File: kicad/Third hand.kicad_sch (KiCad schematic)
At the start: 66 parts, among them U001 74HC595, U002 74HC595

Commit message: First completely routed version
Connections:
- net Px0 renamed Tx0
- net Px1 renamed Tx1
- net Px2 renamed Tx2
- net Px3 renamed Tx3
- net Px4 renamed Tx4
- net Px5 renamed Tx5
- net Px6 renamed Tx6
- net Px7 renamed Tx7
- net Px8 renamed Tx8
- net Px9 renamed Tx9
- net Q0x renamed T0x
- net Q1x renamed T1x
- net Q2x renamed T2x
- net Q3x renamed T3x
- net Q4x renamed T4x
- net Q5x renamed T5x

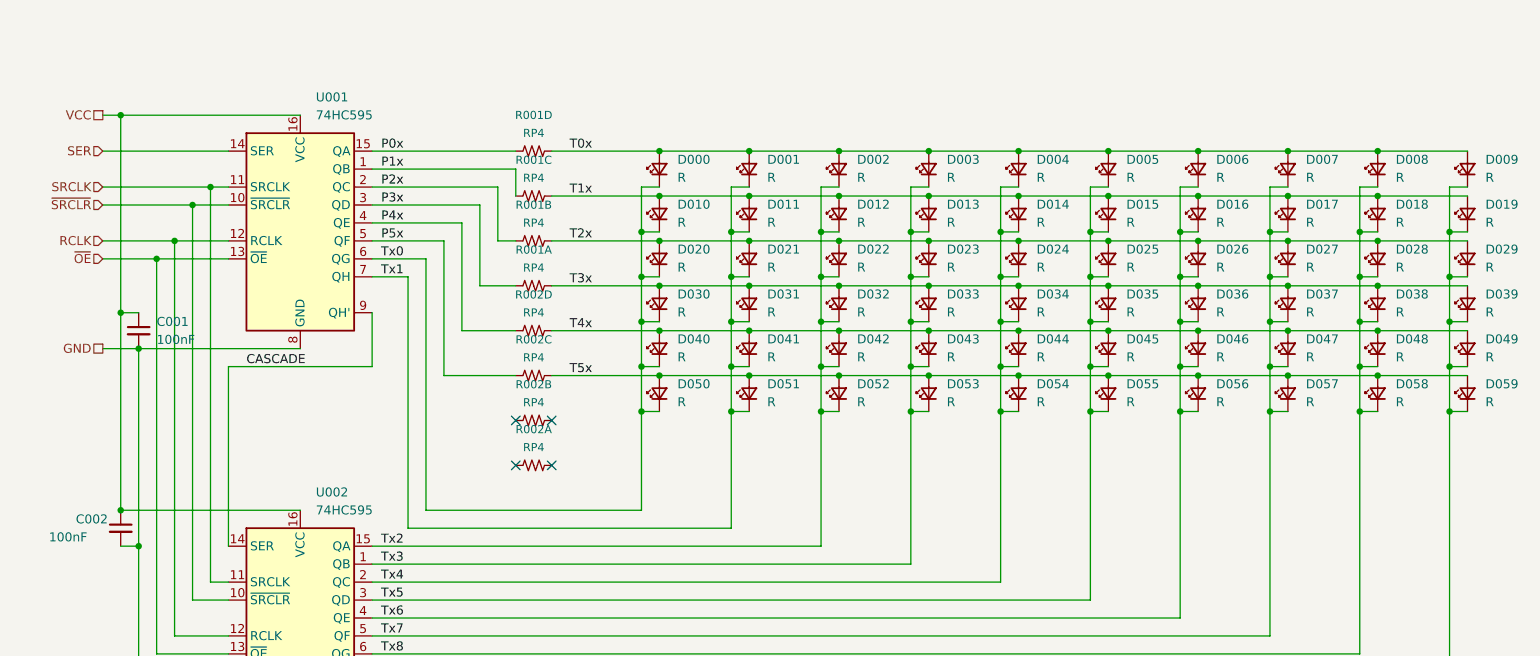
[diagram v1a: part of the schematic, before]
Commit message: Add notes for diode voltages
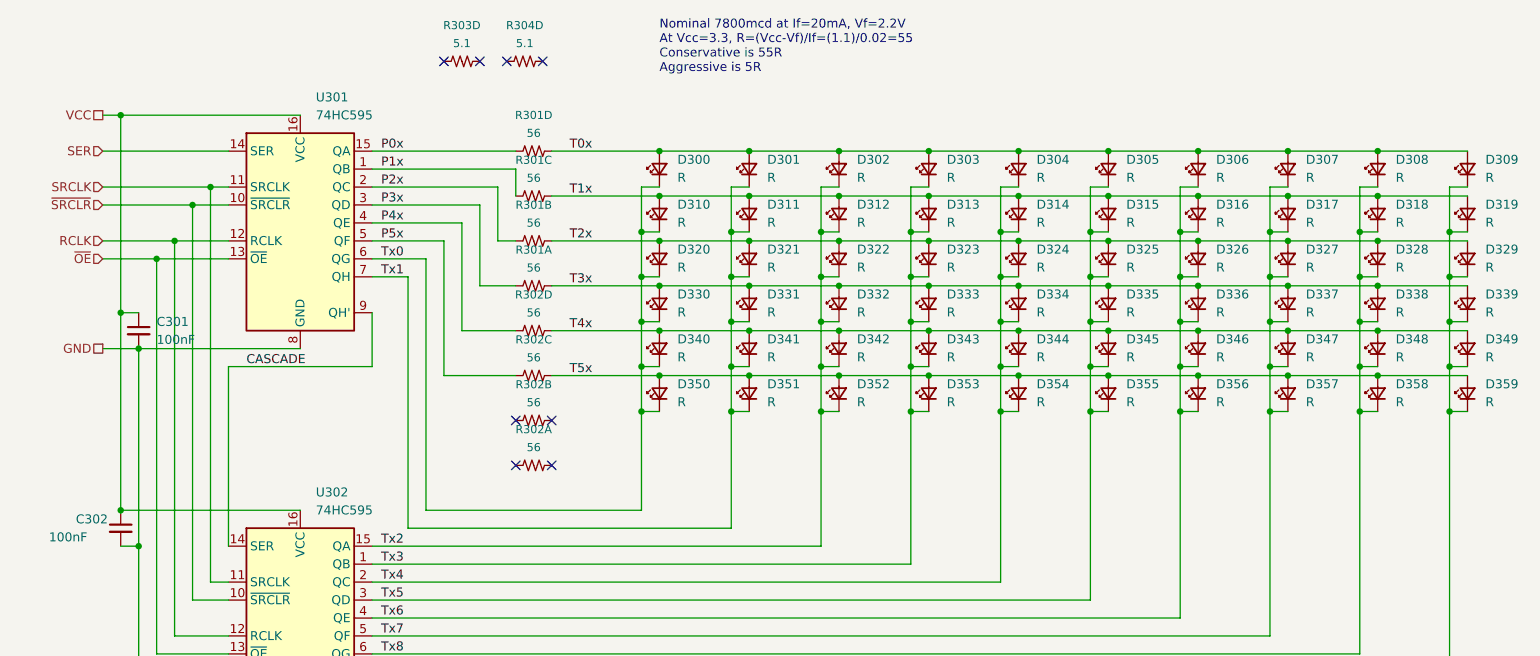
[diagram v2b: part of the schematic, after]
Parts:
- added R303, R304: 5.1, KwanSystems:R_Array_Convex_4x0402, symbol KwanSystems:RP4
- C301: renamed from C001; Digikey (none) -> 445-5613-1-ND; Part Number (none) -> CGA2B1X7R1C104K050BC; Purpose (none) -> Third hand decoder bypass
- C302: renamed from C002; Digikey (none) -> 445-5613-1-ND; Part Number (none) -> CGA2B1X7R1C104K050BC; Purpose (none) -> Third hand decoder bypass
- D300: renamed from D000; Digikey 754-2330-1-ND -> 754-2329-1-ND; Part Number APDA1806SURCK -> APDA1806SECK/J3-PRV; Purpose (none) -> Red third hand
- D301: renamed from D001; Digikey 754-2330-1-ND -> 754-2329-1-ND; Part Number APDA1806SURCK -> APDA1806SECK/J3-PRV; Purpose (none) -> Red third hand
- D302: renamed from D002; Digikey 754-2330-1-ND -> 754-2329-1-ND; Part Number APDA1806SURCK -> APDA1806SECK/J3-PRV; Purpose (none) -> Red third hand
- D303: renamed from D003; Digikey 754-2330-1-ND -> 754-2329-1-ND; Part Number APDA1806SURCK -> APDA1806SECK/J3-PRV; Purpose (none) -> Red third hand
- D304: renamed from D004; Digikey 754-2330-1-ND -> 754-2329-1-ND; Part Number APDA1806SURCK -> APDA1806SECK/J3-PRV; Purpose (none) -> Red third hand
- D305: renamed from D005; Digikey 754-2330-1-ND -> 754-2329-1-ND; Part Number APDA1806SURCK -> APDA1806SECK/J3-PRV; Purpose (none) -> Red third hand
- D306: renamed from D006; Digikey 754-2330-1-ND -> 754-2329-1-ND; Part Number APDA1806SURCK -> APDA1806SECK/J3-PRV; Purpose (none) -> Red third hand
- D307: renamed from D007; Digikey 754-2330-1-ND -> 754-2329-1-ND; Part Number APDA1806SURCK -> APDA1806SECK/J3-PRV; Purpose (none) -> Red third hand
- D308: renamed from D008; Digikey 754-2330-1-ND -> 754-2329-1-ND; Part Number APDA1806SURCK -> APDA1806SECK/J3-PRV; Purpose (none) -> Red third hand
- D309: renamed from D009; Digikey 754-2330-1-ND -> 754-2329-1-ND; Part Number APDA1806SURCK -> APDA1806SECK/J3-PRV; Purpose (none) -> Red third hand
- D310: renamed from D010; Digikey 754-2330-1-ND -> 754-2329-1-ND; Part Number APDA1806SURCK -> APDA1806SECK/J3-PRV; Purpose (none) -> Red third hand
- D311: renamed from D011; Digikey 754-2330-1-ND -> 754-2329-1-ND; Part Number APDA1806SURCK -> APDA1806SECK/J3-PRV; Purpose (none) -> Red third hand
- D312: renamed from D012; Digikey 754-2330-1-ND -> 754-2329-1-ND; Part Number APDA1806SURCK -> APDA1806SECK/J3-PRV; Purpose (none) -> Red third hand
- D313: renamed from D013; Digikey 754-2330-1-ND -> 754-2329-1-ND; Part Number APDA1806SURCK -> APDA1806SECK/J3-PRV; Purpose (none) -> Red third hand
- D314: renamed from D014; Digikey 754-2330-1-ND -> 754-2329-1-ND; Part Number APDA1806SURCK -> APDA1806SECK/J3-PRV; Purpose (none) -> Red third hand
- D315: renamed from D015; Digikey 754-2330-1-ND -> 754-2329-1-ND; Part Number APDA1806SURCK -> APDA1806SECK/J3-PRV; Purpose (none) -> Red third hand
- D316: renamed from D016; Digikey 754-2330-1-ND -> 754-2329-1-ND; Part Number APDA1806SURCK -> APDA1806SECK/J3-PRV; Purpose (none) -> Red third hand
- D317: renamed from D017; Digikey 754-2330-1-ND -> 754-2329-1-ND; Part Number APDA1806SURCK -> APDA1806SECK/J3-PRV; Purpose (none) -> Red third hand
- D318: renamed from D018; Digikey 754-2330-1-ND -> 754-2329-1-ND; Part Number APDA1806SURCK -> APDA1806SECK/J3-PRV; Purpose (none) -> Red third hand
- D319: renamed from D019; Digikey 754-2330-1-ND -> 754-2329-1-ND; Part Number APDA1806SURCK -> APDA1806SECK/J3-PRV; Purpose (none) -> Red third hand
- D320: renamed from D020; Digikey 754-2330-1-ND -> 754-2329-1-ND; Part Number APDA1806SURCK -> APDA1806SECK/J3-PRV; Purpose (none) -> Red third hand
- D321: renamed from D021; Digikey 754-2330-1-ND -> 754-2329-1-ND; Part Number APDA1806SURCK -> APDA1806SECK/J3-PRV; Purpose (none) -> Red third hand
- D322: renamed from D022; Digikey 754-2330-1-ND -> 754-2329-1-ND; Part Number APDA1806SURCK -> APDA1806SECK/J3-PRV; Purpose (none) -> Red third hand
- D323: renamed from D023; Digikey 754-2330-1-ND -> 754-2329-1-ND; Part Number APDA1806SURCK -> APDA1806SECK/J3-PRV; Purpose (none) -> Red third hand
- D324: renamed from D024; Digikey 754-2330-1-ND -> 754-2329-1-ND; Part Number APDA1806SURCK -> APDA1806SECK/J3-PRV; Purpose (none) -> Red third hand
- D325: renamed from D025; Digikey 754-2330-1-ND -> 754-2329-1-ND; Part Number APDA1806SURCK -> APDA1806SECK/J3-PRV; Purpose (none) -> Red third hand
- D326: renamed from D026; Digikey 754-2330-1-ND -> 754-2329-1-ND; Part Number APDA1806SURCK -> APDA1806SECK/J3-PRV; Purpose (none) -> Red third hand
- D327: renamed from D027; Digikey 754-2330-1-ND -> 754-2329-1-ND; Part Number APDA1806SURCK -> APDA1806SECK/J3-PRV; Purpose (none) -> Red third hand
- D328: renamed from D028; Digikey 754-2330-1-ND -> 754-2329-1-ND; Part Number APDA1806SURCK -> APDA1806SECK/J3-PRV; Purpose (none) -> Red third hand
- D329: renamed from D029; Digikey 754-2330-1-ND -> 754-2329-1-ND; Part Number APDA1806SURCK -> APDA1806SECK/J3-PRV; Purpose (none) -> Red third hand
- D330: renamed from D030; Digikey 754-2330-1-ND -> 754-2329-1-ND; Part Number APDA1806SURCK -> APDA1806SECK/J3-PRV; Purpose (none) -> Red third hand
- D331: renamed from D031; Digikey 754-2330-1-ND -> 754-2329-1-ND; Part Number APDA1806SURCK -> APDA1806SECK/J3-PRV; Purpose (none) -> Red third hand
- D332: renamed from D032; Digikey 754-2330-1-ND -> 754-2329-1-ND; Part Number APDA1806SURCK -> APDA1806SECK/J3-PRV; Purpose (none) -> Red third hand
- D333: renamed from D033; Digikey 754-2330-1-ND -> 754-2329-1-ND; Part Number APDA1806SURCK -> APDA1806SECK/J3-PRV; Purpose (none) -> Red third hand
- D334: renamed from D034; Digikey 754-2330-1-ND -> 754-2329-1-ND; Part Number APDA1806SURCK -> APDA1806SECK/J3-PRV; Purpose (none) -> Red third hand
- D335: renamed from D035; Digikey 754-2330-1-ND -> 754-2329-1-ND; Part Number APDA1806SURCK -> APDA1806SECK/J3-PRV; Purpose (none) -> Red third hand
- D336: renamed from D036; Digikey 754-2330-1-ND -> 754-2329-1-ND; Part Number APDA1806SURCK -> APDA1806SECK/J3-PRV; Purpose (none) -> Red third hand
- D337: renamed from D037; Digikey 754-2330-1-ND -> 754-2329-1-ND; Part Number APDA1806SURCK -> APDA1806SECK/J3-PRV; Purpose (none) -> Red third hand
- D338: renamed from D038; Digikey 754-2330-1-ND -> 754-2329-1-ND; Part Number APDA1806SURCK -> APDA1806SECK/J3-PRV; Purpose (none) -> Red third hand
- D339: renamed from D039; Digikey 754-2330-1-ND -> 754-2329-1-ND; Part Number APDA1806SURCK -> APDA1806SECK/J3-PRV; Purpose (none) -> Red third hand
- D340: renamed from D040; Digikey 754-2330-1-ND -> 754-2329-1-ND; Part Number APDA1806SURCK -> APDA1806SECK/J3-PRV; Purpose (none) -> Red third hand
- D341: renamed from D041; Digikey 754-2330-1-ND -> 754-2329-1-ND; Part Number APDA1806SURCK -> APDA1806SECK/J3-PRV; Purpose (none) -> Red third hand
- D342: renamed from D042; Digikey 754-2330-1-ND -> 754-2329-1-ND; Part Number APDA1806SURCK -> APDA1806SECK/J3-PRV; Purpose (none) -> Red third hand
- D343: renamed from D043; Digikey 754-2330-1-ND -> 754-2329-1-ND; Part Number APDA1806SURCK -> APDA1806SECK/J3-PRV; Purpose (none) -> Red third hand
- D344: renamed from D044; Digikey 754-2330-1-ND -> 754-2329-1-ND; Part Number APDA1806SURCK -> APDA1806SECK/J3-PRV; Purpose (none) -> Red third hand
- D345: renamed from D045; Digikey 754-2330-1-ND -> 754-2329-1-ND; Part Number APDA1806SURCK -> APDA1806SECK/J3-PRV; Purpose (none) -> Red third hand
- D346: renamed from D046; Digikey 754-2330-1-ND -> 754-2329-1-ND; Part Number APDA1806SURCK -> APDA1806SECK/J3-PRV; Purpose (none) -> Red third hand
- D347: renamed from D047; Digikey 754-2330-1-ND -> 754-2329-1-ND; Part Number APDA1806SURCK -> APDA1806SECK/J3-PRV; Purpose (none) -> Red third hand
- D348: renamed from D048; Digikey 754-2330-1-ND -> 754-2329-1-ND; Part Number APDA1806SURCK -> APDA1806SECK/J3-PRV; Purpose (none) -> Red third hand
- D349: renamed from D049; Digikey 754-2330-1-ND -> 754-2329-1-ND; Part Number APDA1806SURCK -> APDA1806SECK/J3-PRV; Purpose (none) -> Red third hand
- D350: renamed from D050; Digikey 754-2330-1-ND -> 754-2329-1-ND; Part Number APDA1806SURCK -> APDA1806SECK/J3-PRV; Purpose (none) -> Red third hand
- D351: renamed from D051; Digikey 754-2330-1-ND -> 754-2329-1-ND; Part Number APDA1806SURCK -> APDA1806SECK/J3-PRV; Purpose (none) -> Red third hand
- D352: renamed from D052; Digikey 754-2330-1-ND -> 754-2329-1-ND; Part Number APDA1806SURCK -> APDA1806SECK/J3-PRV; Purpose (none) -> Red third hand
- D353: renamed from D053; Digikey 754-2330-1-ND -> 754-2329-1-ND; Part Number APDA1806SURCK -> APDA1806SECK/J3-PRV; Purpose (none) -> Red third hand
- D354: renamed from D054; Digikey 754-2330-1-ND -> 754-2329-1-ND; Part Number APDA1806SURCK -> APDA1806SECK/J3-PRV; Purpose (none) -> Red third hand
- D355: renamed from D055; Digikey 754-2330-1-ND -> 754-2329-1-ND; Part Number APDA1806SURCK -> APDA1806SECK/J3-PRV; Purpose (none) -> Red third hand
- D356: renamed from D056; Digikey 754-2330-1-ND -> 754-2329-1-ND; Part Number APDA1806SURCK -> APDA1806SECK/J3-PRV; Purpose (none) -> Red third hand
- D357: renamed from D057; Digikey 754-2330-1-ND -> 754-2329-1-ND; Part Number APDA1806SURCK -> APDA1806SECK/J3-PRV; Purpose (none) -> Red third hand
- D358: renamed from D058; Digikey 754-2330-1-ND -> 754-2329-1-ND; Part Number APDA1806SURCK -> APDA1806SECK/J3-PRV; Purpose (none) -> Red third hand
- D359: renamed from D059; Digikey 754-2330-1-ND -> 754-2329-1-ND; Part Number APDA1806SURCK -> APDA1806SECK/J3-PRV; Purpose (none) -> Red third hand
- R301: renamed from R001; value RP4 -> 56; Digikey (none) -> Y7560CT-ND; Part Number (none) -> EXB-28V560JX; Purpose (none) -> Third hand conservative current limit
- R302: renamed from R002; value RP4 -> 56; Digikey (none) -> Y7560CT-ND; Part Number (none) -> EXB-28V560JX; Purpose (none) -> Third hand conservative current limit
- U301: renamed from U001; Part Number (none) -> 74HC595PW,118; Purpose (none) -> Hand Decoder
- U302: renamed from U002; Part Number (none) -> 74HC595PW,118; Purpose (none) -> Hand Decoder
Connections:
- no-connect marks 4 -> 8
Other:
- note added: "Nominal 7800mcd at If=20mA, Vf=2.2V At Vcc=3.3, R=(Vcc-Vf)/If=(1.1)/0.02=55 Conservative is 55R Aggressive is 5R"

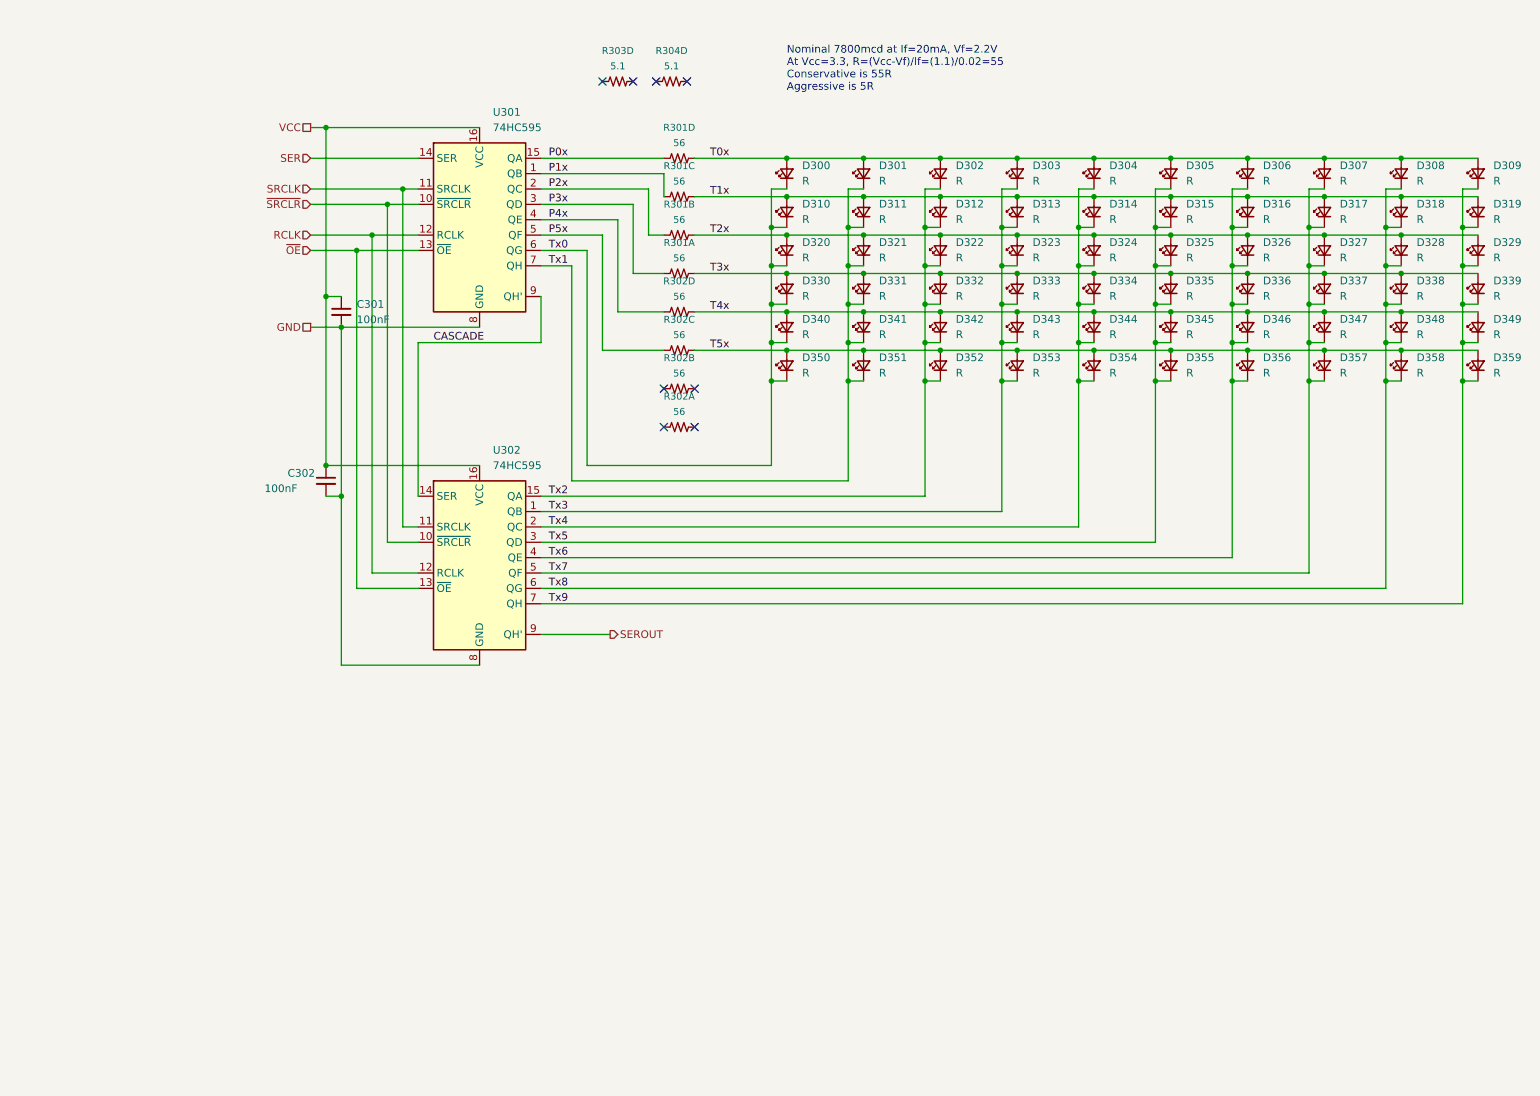
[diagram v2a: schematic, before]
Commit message: Put MOSFET switch transistors in place. We won't end up using these.
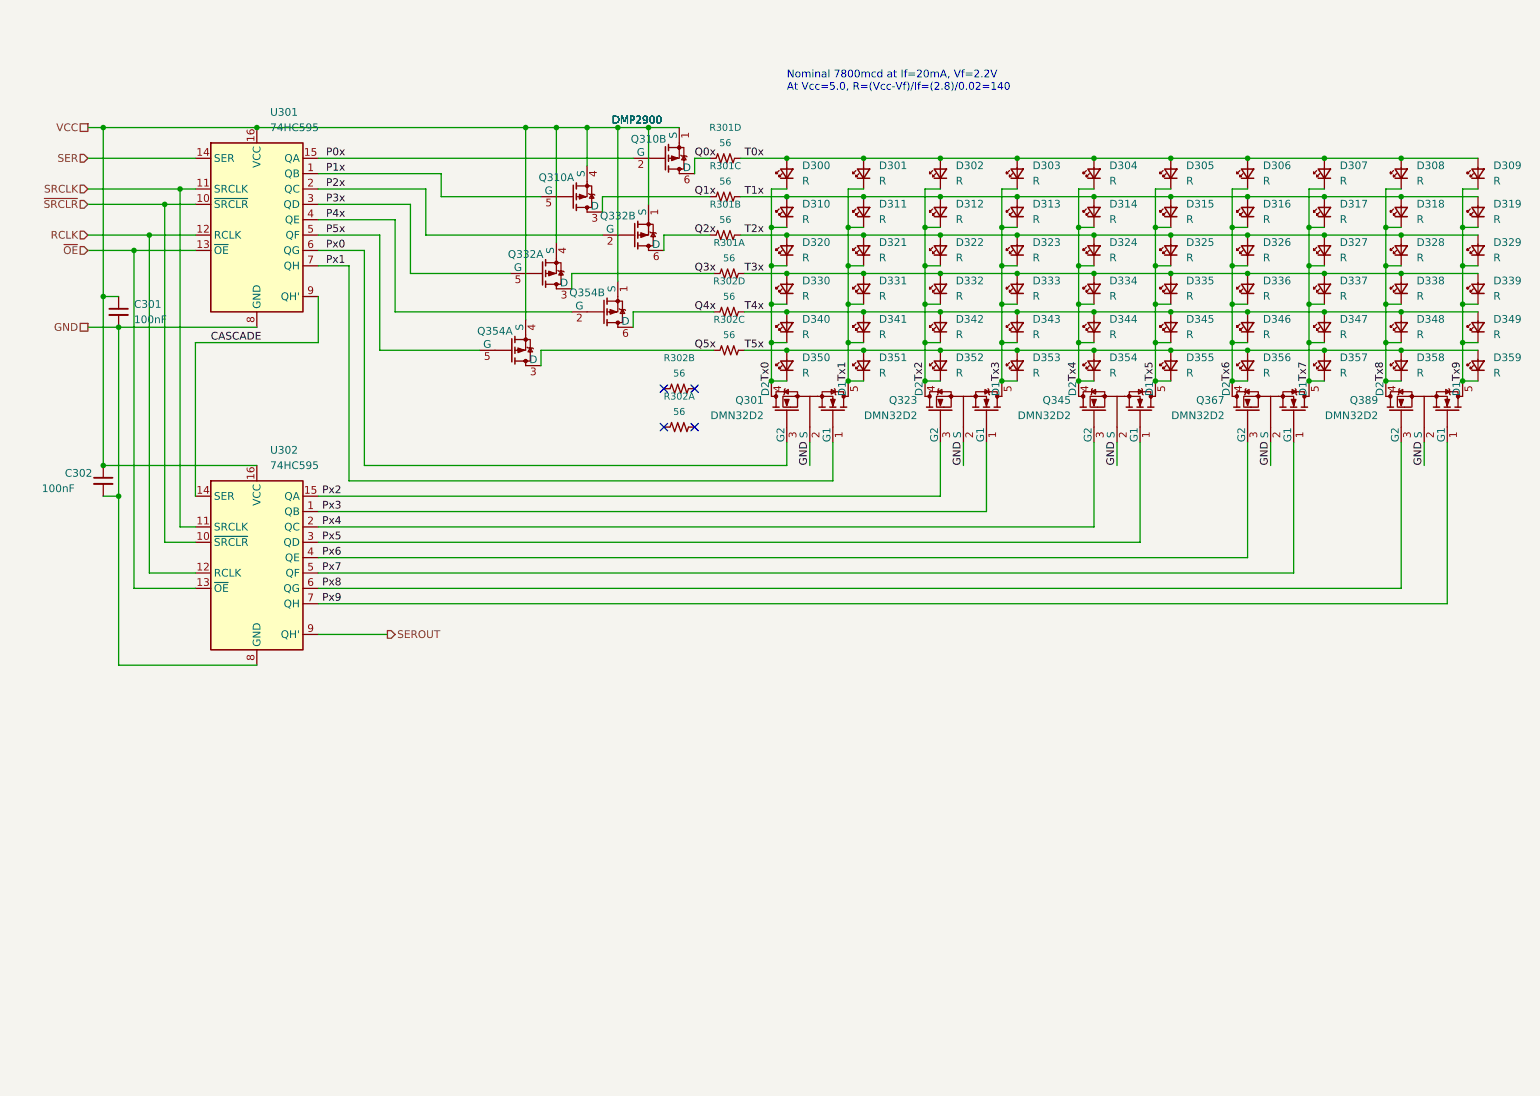
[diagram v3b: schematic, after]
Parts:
- removed R303, R304: 5.1, KwanSystems:R_Array_Convex_4x0402, symbol KwanSystems:RP4
- added Q301, Q323, Q345, Q367, Q389: DMN32D2, Package_TO_SOT_SMD:SOT-353_SC-70-5, symbol KwanSystems:NMOS_DUAL_COMMON_SOURCE
- added Q310, Q332, Q354: DMP2900, Package_TO_SOT_SMD:SOT-363_SC-70-6, symbol KwanSystems:PMOS_DUAL
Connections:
- net GND: now also Q301.2 (S), Q323.2 (S), Q345.2 (S), Q367.2 (S), Q389.2 (S)
- net P0x: now also Q310.2 (G); no longer R301.4
- net P1x: now also Q310.5 (G); no longer R301.3 (4)
- net P2x: now also Q332.2 (G); no longer R301.2 (4)
- net P3x: now also Q332.5 (G); no longer R301.1 (4)
- net P4x: now also Q354.2 (G); no longer R302.4
- net P5x: now also Q354.5 (G); no longer R302.3 (4)
- net Tx0: now also Q301.4 (D2); no longer U301.6 (QG)
- net Tx1: now also Q301.5 (D1); no longer U301.7 (QH)
- net Tx2: now also Q323.4 (D2); no longer U302.15 (QA)
- net Tx3: now also Q323.5 (D1); no longer U302.1 (QB)
- net Tx4: now also Q345.4 (D2); no longer U302.2 (QC)
- net Tx5: now also Q345.5 (D1); no longer U302.3 (QD)
- net Tx6: now also Q367.4 (D2); no longer U302.4 (QE)
- net Tx7: now also Q367.5 (D1); no longer U302.5 (QF)
- net Tx8: now also Q389.4 (D2); no longer U302.6 (QG)
- net Tx9: now also Q389.5 (D1); no longer U302.7 (QH)
- net VCC: now also Q310.1 (S), Q310.4 (S), Q332.1 (S), Q332.4 (S), Q354.1 (S), Q354.4 (S)
- new net Px0: Q301.3 (G2), U301.6 (QG)
- new net Px1: Q301.1 (G1), U301.7 (QH)
- new net Px2: Q323.3 (G2), U302.15 (QA)
- new net Px3: Q323.1 (G1), U302.1 (QB)
- new net Px4: Q345.3 (G2), U302.2 (QC)
- new net Px5: Q345.1 (G1), U302.3 (QD)
- new net Px6: Q367.3 (G2), U302.4 (QE)
- new net Px7: Q367.1 (G1), U302.5 (QF)
- new net Px8: Q389.3 (G2), U302.6 (QG)
- new net Px9: Q389.1 (G1), U302.7 (QH)
- new net Q0x: Q310.6 (D), R301.4
- new net Q1x: Q310.3 (D), R301.3 (4)
- new net Q2x: Q332.6 (D), R301.2 (4)
- new net Q3x: Q332.3 (D), R301.1 (4)
- new net Q4x: Q354.6 (D), R302.4
- new net Q5x: Q354.3 (D), R302.3 (4)
- no-connect marks 8 -> 4
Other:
- note added: "Nominal 7800mcd at If=20mA, Vf=2.2V At Vcc=5.0, R=(Vcc-Vf)/If=(2.8)/0.02=140"
- note removed: "Nominal 7800mcd at If=20mA, Vf=2.2V At Vcc=3.3, R=(Vcc-Vf)/If=(1.1)/0.02=55 Conservative is 55R Aggressive is 5R"
- moved on the sheet: C301, C302, R301A, R301B, R301C, R301D, R302C, R302D, U301, U302
